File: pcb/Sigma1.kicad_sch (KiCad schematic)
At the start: 60 parts, among them J1 Conn_01x02, J10 Screw_Terminal_01x02, J11 Screw_Terminal_01x02, J2 Screw_Terminal_01x02, J3 Servo 1, J4 Servo 2, J5 Servo 3, J6 Servo 1, J8 Conn_01x10, J9 Screw_Terminal_01x02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

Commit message: supply chain changes
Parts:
- removed SW1, SW2: SW_Push, Button_Switch_SMD:SW_SPST_B3U-1000P-B, symbol Switch:SW_Push
- removed U4: MS5611-01BA, Package_LGA:LGA-8_3x5mm_P1.25mm, symbol Sensor_Pressure:MS5611-01BA
- removed U5: MLX90395xLW, Package_DFN_QFN:QFN-16-1EP_3x3mm_P0.5mm_EP1.675x1.675mm, symbol Sensor_Magnetic:MLX90395xLW
- added C6: 100n, Capacitor_SMD:C_0603_1608Metric, symbol Device:C
- added SW1, SW3: TS-1088R-02026, easyeda2kicad:SW-SMD_L3.9-W3.0-P4.45, symbol easyeda2kicad:TS-1088R-02026
- added U5: BMP390_C5124834, easyeda2kicad:LGA-10_L2.0-W2.0-P0.50-BL, symbol easyeda2kicad:BMP390_C5124834
- added U7: MLX90395KDC-BBA-001-SP, MLX90395KDC-BBA-001-SP:SOIC127P600X172-8N, symbol MLX90395KDC-BBA-001-SP:MLX90395KDC-BBA-001-SP
- C19: renamed from C6; value C -> 10uf
- C5: value C -> 0.1μF
- J3, J4, J5, J6: footprint Connector_PinHeader_2.54mm:PinHeader_1x03_P2.54mm_Vertical_SMD_Pin1Left -> Connector_PinHeader_2.54mm:PinHeader_1x03_P2.54mm_Vertical
- J8: footprint Connector_PinSocket_2.54mm:PinSocket_1x10_P2.54mm_Vertical_SMD_Pin1Left -> Connector_PinHeader_2.54mm:PinHeader_1x10_P2.54mm_Vertical
- R4: value 350 -> 330
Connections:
- net BARO_CS: now also U5.6 (CSB)
- net GND: now also C19.2, C6.2, SW1.1, SW3.1, U5.3 (VSS), U5.8 (VSS), U5.9 (VSS), U7.6 (VSS); no longer C19.1
- net MAG_CS: now also U7.8 (MS/CS)
- net SPI_MISO: now also U5.5 (SDO), U7.3 (MISO)
- net SPI_MOSI: now also U5.4 (SDI), U7.2 (SDA/MOSI)
- net SPI_SCLK: now also U5.2 (SCK), U7.1 (SCL/SCLK)
- net VCC: now also C19.1, C6.1, U5.1 (VDDIO), U5.10 (VDD), U7.7 (VDD); no longer C19.2
- net at C4.1, U1.27 (IO0): now also SW1.2
- net at C3.1, R2.2, U1.3 (EN): now also SW3.2
- no-connect marks 11 -> 10
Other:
- moved on the sheet: C11

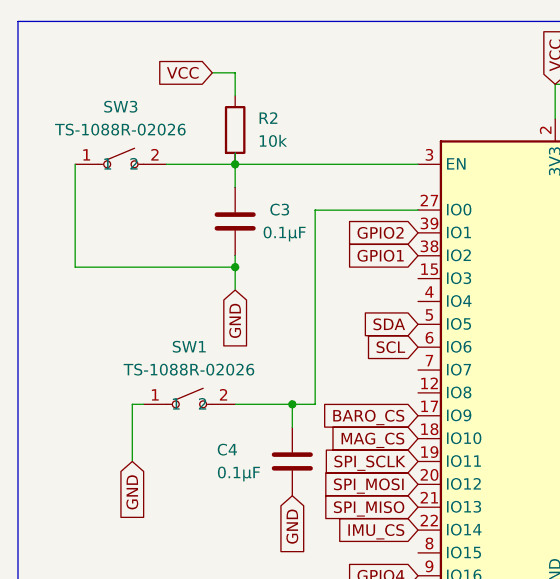
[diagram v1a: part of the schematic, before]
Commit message: BOM + supply chain changes
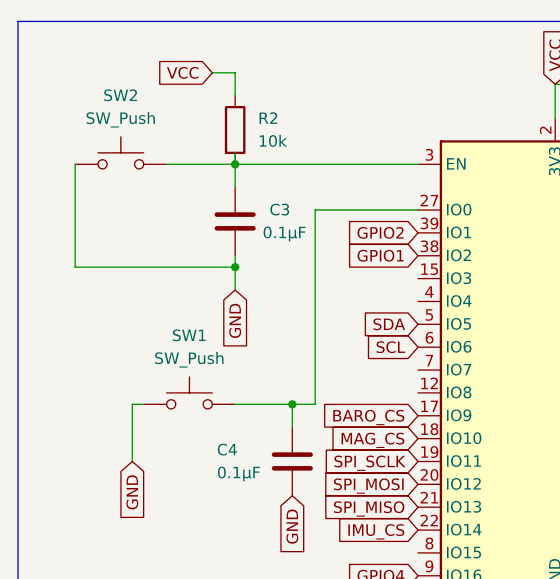
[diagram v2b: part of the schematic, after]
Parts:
- removed SW1, SW3: TS-1088R-02026, easyeda2kicad:SW-SMD_L3.9-W3.0-P4.45, symbol easyeda2kicad:TS-1088R-02026
- added SW1, SW2: SW_Push, TL3365AF180QG:SW_TL3365AF180QG, symbol Switch:SW_Push
- P1: footprint Connector_USB:USB_C_Receptacle_HRO_TYPE-C-31-M-12 -> Connector_USB:USB_C_Receptacle_Amphenol_124019772112A
- U7: footprint MLX90395KDC-BBA-001-SP:SOIC127P600X172-8N -> MLX90395KDC-BBA-101-SP:SOIC127P600X172-8N
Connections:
- net GND: now also SW1.1, SW2.1
- net at C3.1, R2.2, U1.3 (EN): now also SW2.2
- net at C4.1, U1.27 (IO0): now also SW1.2
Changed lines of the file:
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@@
 	)
 	(symbol
+		(lib_id "Switch:SW_Push")
+		(at 38.1 76.2 0)
+		(unit 1)
+		(exclude_from_sim no)
+		(in_bom yes)
+		(on_board yes)
+		(dnp no)
+		(fields_autoplaced yes)
+		(property "Reference" "SW1"
+			(at 38.1 68.58 0)
+			(effects
+				(font
+					(size 1.27 1.27)
+				)
+			)
+		)
+		(property "Value" "SW_Push"
+			(at 38.1 71.12 0)
+			(effects
+				(font
+					(size 1.27 1.27)
+				)
+			)
+		)
+		(property "Footprint" "TL3365AF180QG:SW_TL3365AF180QG"
+			(at 38.1 71.12 0)
+			(effects
+				(font
+					(size 1.27 1.27)
+				)
+				(hide yes)
+			)
+		)
+		(property "Datasheet" "~"
+			(at 38.1 71.12 0)
+			(effects
+				(font
+					(size 1.27 1.27)
+				)
+				(hide yes)
+			)
+		)
+		(property "Description" "Push button switch, generic, two pins"
+			(at 38.1 76.2 0)
+			(effects
+				(font
+					(size 1.27 1.27)
+				)
+				(hide yes)
+			)
+		)
+		(pin "2"
+		)
+		(pin "1"
+		)
+		(instances
+			(project "Sigma1"
+				(path "/86cf4319-5abb-4674-bb55-c16ab4b96581"
+					(reference "SW1")
+					(unit 1)
+				)
+			)
+		)
+	)
+	(symbol
 		(lib_id "Device:C")
 		(at 142.24 128.27 0)
@@
 			)
 		)
-		(property "Footprint" "Connector_USB:USB_C_Receptacle_HRO_TYPE-C-31-M-12"
+		(property "Footprint" "Connector_USB:USB_C_Receptacle_Amphenol_124019772112A"
 			(at 41.91 156.21 0)
 			(effects
@@
 	)
 	(symbol
+		(lib_id "Switch:SW_Push")
+		(at 30.48 49.53 0)
+		(unit 1)
+		(exclude_from_sim no)
+		(in_bom yes)
+		(on_board yes)
+		(dnp no)
+		(fields_autoplaced yes)
+		(property "Reference" "SW2"
+			(at 30.48 41.91 0)
+			(effects
+				(font
+					(size 1.27 1.27)
+				)
+			)
+		)
+		(property "Value" "SW_Push"
+			(at 30.48 44.45 0)
+			(effects
+				(font
+					(size 1.27 1.27)
+				)
+			)
+		)
+		(property "Footprint" "TL3365AF180QG:SW_TL3365AF180QG"
+			(at 30.48 44.45 0)
+			(effects
+				(font
+					(size 1.27 1.27)
+				)
+				(hide yes)
+			)
+		)
+		(property "Datasheet" "~"
+			(at 30.48 44.45 0)
+			(effects
+				(font
+					(size 1.27 1.27)
+				)
+				(hide yes)
+			)
+		)
+		(property "Description" "Push button switch, generic, two pins"
+			(at 30.48 49.53 0)
+			(effects
+				(font
+					(size 1.27 1.27)
+				)
+				(hide yes)
+			)
+		)
+		(pin "2"
+		)
+		(pin "1"
+		)
+		(instances
+			(project ""
+				(path "/86cf4319-5abb-4674-bb55-c16ab4b96581"
+					(reference "SW2")
+					(unit 1)
+				)
+			)
+		)
+	)
+	(symbol
 		(lib_id "Device:R")
 		(at 57.15 146.05 90)
@@
 			)
 		)
-		(property "Footprint" "MLX90395KDC-BBA-001-SP:SOIC127P600X172-8N"
+		(property "Footprint" "MLX90395KDC-BBA-101-SP:SOIC127P600X172-8N"
 			(at 309.88 53.34 0)
 			(effects
@@
 	)
 	(symbol
-		(lib_id "easyeda2kicad:TS-1088R-02026")
-		(at 38.1 76.2 0)
-		(unit 1)
-		(exclude_from_sim no)
-		(in_bom yes)
-		(on_board yes)
-		(dnp no)
-		(fields_autoplaced yes)
-		(property "Reference" "SW1"
-			(at 38.1 69.85 0)
-			(effects
-				(font
-					(size 1.27 1.27)
-				)
-			)
-		)
-		(property "Value" "TS-1088R-02026"
-			(at 38.1 72.39 0)
-			(effects
-				(font
-					(size 1.27 1.27)
-				)
-			)
-		)
-		(property "Footprint" "easyeda2kicad:SW-SMD_L3.9-W3.0-P4.45"
-			(at 38.1 83.82 0)
-			(effects
-				(font
-					(size 1.27 1.27)
-				)
-				(hide yes)
-			)
-		)
-		(property "Datasheet" "https://lcsc.com/product-detail/New-Arrivals_XUNPU-TS-1088R-02026_C455280.html"
-			(at 38.1 86.36 0)
-			(effects
-				(font
-					(size 1.27 1.27)
-				)
-				(hide yes)
-			)
-		)
-		(property "Description" ""
-			(at 38.1 76.2 0)
-			(effects
-				(font
-					(size 1.27 1.27)
-				)
-				(hide yes)
-			)
-		)
-		(property "LCSC Part" "C455280"
-			(at 38.1 88.9 0)
-			(effects
-				(font
-					(size 1.27 1.27)
-				)
-				(hide yes)
-			)
-		)
-		(pin "1"
-		)
-		(pin "2"
-		)
-		(instances
-			(project ""
-				(path "/86cf4319-5abb-4674-bb55-c16ab4b96581"
-					(reference "SW1")
-					(unit 1)
-				)
-			)
-		)
-	)
-	(symbol
 		(lib_id "Device:R")
 		(at 132.08 143.51 0)
@@
 					(unit 1)
 				)
-			)
-		)
-	)
-	(symbol
-		(lib_id "easyeda2kicad:TS-1088R-02026")
-		(at 30.48 49.53 0)
-		(unit 1)
-		(exclude_from_sim no)
-		(in_bom yes)
-		(on_board yes)
-		(dnp no)
-		(fields_autoplaced yes)
-		(property "Reference" "SW3"
-			(at 30.48 43.18 0)
-			(effects
-				(font
-					(size 1.27 1.27)
-				)
-			)
-		)
-		(property "Value" "TS-1088R-02026"
-			(at 30.48 45.72 0)
-			(effects
-				(font
-					(size 1.27 1.27)
-				)
-			)
-		)
-		(property "Footprint" "easyeda2kicad:SW-SMD_L3.9-W3.0-P4.45"
-			(at 30.48 57.15 0)
-			(effects
-				(font
-					(size 1.27 1.27)
-				)
-				(hide yes)
-			)
-		)
-		(property "Datasheet" "https://lcsc.com/product-detail/New-Arrivals_XUNPU-TS-1088R-02026_C455280.html"
-			(at 30.48 59.69 0)
-			(effects
-				(font
-					(size 1.27 1.27)
-				)
-				(hide yes)
-			)
-		)
-		(property "Description" ""
-			(at 30.48 49.53 0)
-			(effects
-				(font
-					(size 1.27 1.27)
-				)
-				(hide yes)
-			)
-		)
-		(property "LCSC Part" "C455280"
-			(at 30.48 62.23 0)
-			(effects
-				(font
-					(size 1.27 1.27)
-				)
-				(hide yes)
-			)
-		)
-		(pin "2"
-		)
-		(pin "1"
-		)
-		(instances
-			(project ""
-				(path "/86cf4319-5abb-4674-bb55-c16ab4b96581"
-					(reference "SW3")
-					(unit 1)
-				)

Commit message: fix conflict?
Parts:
- added L1: 3.3uh, Inductor_SMD:L_0805_2012Metric, symbol Device:L
- R3: value 60 -> 10k
- R4: value 330 -> 54.9k
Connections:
- net +5V: now also L1.1; no longer C18.1, U6.2 (SW)
- new net: C18.1, L1.2, U6.2 (SW)
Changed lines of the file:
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@@
 	)
 	(junction
-		(at 142.24 124.46)
-		(diameter 0)
-		(color 0 0 0 0)
-	)
-	(junction
 		(at 273.05 119.38)
 		(diameter 0)
@@
 	)
 	(junction
-		(at 154.94 124.46)
+		(at 152.4 49.53)
 		(diameter 0)
 		(color 0 0 0 0)
 	)
 	(junction
-		(at 152.4 49.53)
+		(at 251.46 73.66)
 		(diameter 0)
 		(color 0 0 0 0)
 	)
 	(junction
-		(at 251.46 73.66)
+		(at 142.24 124.46)
 		(diameter 0)
 		(color 0 0 0 0)
@@
 	)
 	(junction
+		(at 154.94 124.46)
+		(diameter 0)
+		(color 0 0 0 0)
+	)
+	(junction
 		(at 312.42 109.22)
 		(diameter 0)
@@
 		)
 	)
-	(bus_entry
-		(at 118.11 152.4)
-		(size 2.54 2.54)
-		(stroke
-			(width 0)
-			(type default)
-		)
-	)
-	(bus_entry
-		(at 132.08 139.7)
-		(size 2.54 2.54)
-		(stroke
-			(width 0)
-			(type default)
-		)
-	)
 	(wire
 		(pts
@@
 	(wire
 		(pts
-			(xy 151.13 139.7) (xy 153.67 139.7)
+			(xy 142.24 132.08) (xy 139.7 132.08)
 		)
 		(stroke
@@
 	(wire
 		(pts
-			(xy 142.24 132.08) (xy 139.7 132.08)
+			(xy 251.46 66.04) (xy 251.46 68.58)
 		)
 		(stroke
@@
 	(wire
 		(pts
-			(xy 251.46 66.04) (xy 251.46 68.58)
+			(xy 151.13 139.7) (xy 153.67 139.7)
 		)
 		(stroke
@@
 	(wire
 		(pts
+			(xy 152.4 124.46) (xy 154.94 124.46)
+		)
+		(stroke
+			(width 0)
+			(type default)
+		)
+	)
+	(wire
+		(pts
 			(xy 43.18 39.37) (xy 43.18 41.91)
 		)
@@
 	(wire
 		(pts
+			(xy 142.24 124.46) (xy 144.78 124.46)
+		)
+		(stroke
+			(width 0)
+			(type default)
+		)
+	)
+	(wire
+		(pts
 			(xy 43.18 49.53) (xy 43.18 48.26)
 		)
@@
 	(wire
 		(pts
-			(xy 142.24 124.46) (xy 154.94 124.46)
-		)
-		(stroke
-			(width 0)
-			(type default)
-		)
-	)
-	(wire
-		(pts
 			(xy 361.95 109.22) (xy 363.22 109.22)
 		)
@@
 	)
 	(symbol
+		(lib_id "Device:L")
+		(at 148.59 124.46 270)
+		(mirror x)
+		(unit 1)
+		(exclude_from_sim no)
+		(in_bom yes)
+		(on_board yes)
+		(dnp no)
+		(property "Reference" "L1"
+			(at 148.59 119.38 90)
+			(effects
+				(font
+					(size 1.27 1.27)
+				)
+			)
+		)
+		(property "Value" "3.3uh"
+			(at 148.59 121.92 90)
+			(effects
+				(font
+					(size 1.27 1.27)
+				)
+			)
+		)
+		(property "Footprint" "Inductor_SMD:L_0805_2012Metric"
+			(at 148.59 124.46 0)
+			(effects
+				(font
+					(size 1.27 1.27)
+				)
+				(hide yes)
+			)
+		)
+		(property "Datasheet" "~"
+			(at 148.59 124.46 0)
+			(effects
+				(font
+					(size 1.27 1.27)
+				)
+				(hide yes)
+			)
+		)
+		(property "Description" "Inductor"
+			(at 148.59 124.46 0)
+			(effects
+				(font
+					(size 1.27 1.27)
+				)
+				(hide yes)
+			)
+		)
+		(pin "2"
+		)
+		(pin "1"
+		)
+		(instances
+			(project ""
+				(path "/86cf4319-5abb-4674-bb55-c16ab4b96581"
+					(reference "L1")
+					(unit 1)
+				)
+			)
+		)
+	)
+	(symbol
 		(lib_id "Switch:SW_Push")
 		(at 30.48 49.53 0)
@@
 			)
 		)
-		(property "Value" "60"
+		(property "Value" "10k"
 			(at 134.62 144.7799 0)
 			(effects
@@
 			)
 		)
-		(property "Value" "330"
+		(property "Value" "54.9k"
 			(at 147.32 137.16 90)
 			(effects
